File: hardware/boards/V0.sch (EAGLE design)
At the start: 139 parts, among them IC2 TPS6300, J1 SJ-43515TS-SMT, J2 HIROSE_DM3BT-DSF-PEJSHIROSE_D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, J3 MOLEX_105450-0101MOLEX_105450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, Q2 ON_SEMI_MMBT5551LT1GON_SEMI_M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, U1 VS1053-L, U2 MICROCHIP_MCP73831T-2ATI-OTMI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, X3 FH12-45S-0.5SH

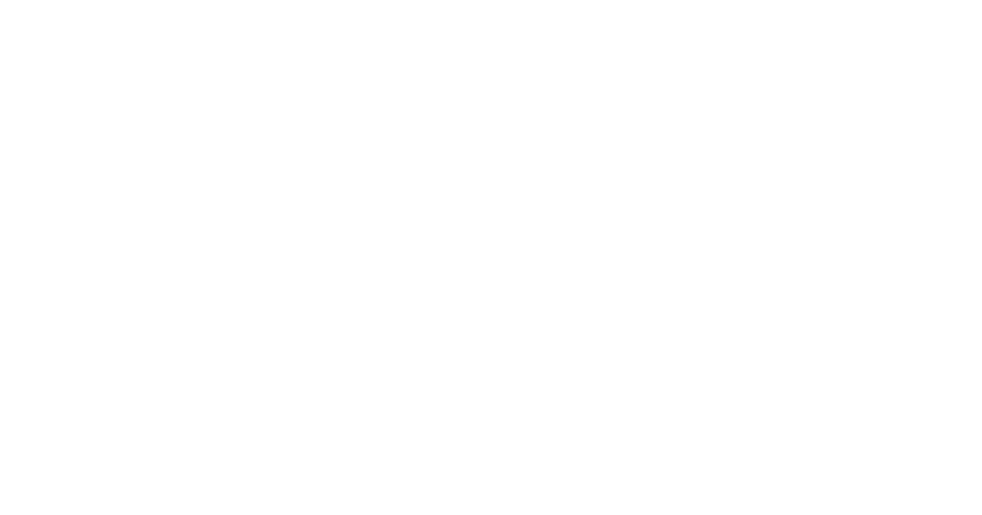
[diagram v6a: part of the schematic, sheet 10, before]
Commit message: Add charge detect back in, using up all our pins
Closes #11
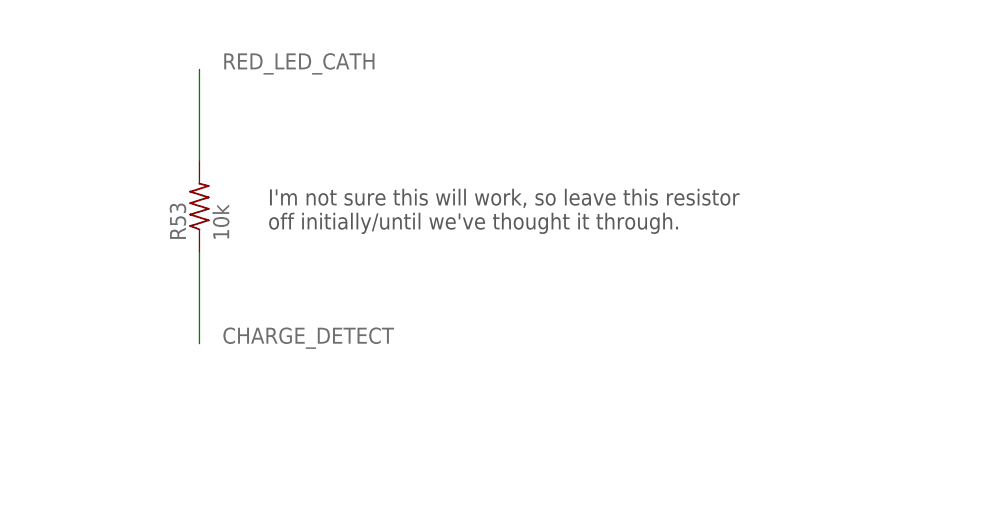
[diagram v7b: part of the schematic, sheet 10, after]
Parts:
- added R53: 10k, rcl:R-US_R0805
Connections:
- new net CHARGE_DETECT: R53.1, U$1.SENSOR_CAPP
- net RED_LED_CATH: now also R53.2
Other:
- note added: "I'm not sure this will work, so leave this resistor off initially/until we've thought it through."
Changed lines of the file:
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@@
 <part name="C36" library="rcl" library_urn="urn:adsk.eagle:library:334" deviceset="C-US" device="C1206" package3d_urn="urn:adsk.eagle:package:23618/2" value="100nF"/>
 <part name="GND48" library="supply1" library_urn="urn:adsk.eagle:library:371" deviceset="GND" device=""/>
+<part name="R53" library="rcl" library_urn="urn:adsk.eagle:library:334" deviceset="R-US_" device="R0805" package3d_urn="urn:adsk.eagle:package:23553/2" value="10k"/>
 </parts>
 <sheets>
@@
 </segment>
 </net>
+<net name="CHARGE_DETECT" class="0">
+<segment>
+<pinref part="U$1" gate="G$1" pin="SENSOR_CAPP"/>
+<wire x1="-50.8" y1="2.54" x2="-55.88" y2="2.54" width="0.1524" layer="91"/>
+<label x="-53.594" y="1.016" size="1.778" layer="95" rot="R180"/>
+</segment>
+</net>
 </nets>
 </sheet>
@@
 1.0 volts for 20mA = V / I = R = 1 / 20mA = 50 ohms</text>
 <text x="-38.1" y="-38.1" size="1.778" layer="97">Blue has a voltage drop of ~3.7V which is greater than our regulated voltage so we won't bother with a current limiting resistor.</text>
+<text x="106.68" y="12.7" size="1.778" layer="97">I'm not sure this will work, so leave this resistor
+off initially/until we've thought it through.</text>
 </plain>
 <instances>
@@
 <attribute name="VALUE" x="-80.518" y="-13.97" size="1.778" layer="96" rot="R90"/>
 </instance>
+<instance part="R53" gate="G$1" x="99.06" y="15.24" smashed="yes" rot="R90">
+<attribute name="NAME" x="97.5614" y="11.43" size="1.778" layer="95" rot="R90"/>
+<attribute name="VALUE" x="102.362" y="11.43" size="1.778" layer="96" rot="R90"/>
+</instance>
 </instances>
 <busses>
@@
 <label x="7.62" y="0" size="1.778" layer="95"/>
 </segment>
+<segment>
+<wire x1="99.06" y1="30.48" x2="99.06" y2="20.32" width="0.1524" layer="91"/>
+<pinref part="R53" gate="G$1" pin="2"/>
+<label x="101.6" y="30.48" size="1.778" layer="95"/>
+</segment>
 </net>
 <net name="N$56" class="0">
@@
 </segment>
 </net>
+<net name="CHARGE_DETECT" class="0">
+<segment>
+<pinref part="R53" gate="G$1" pin="1"/>
+<wire x1="99.06" y1="10.16" x2="99.06" y2="0" width="0.1524" layer="91"/>
+<label x="101.6" y="0" size="1.778" layer="95"/>
+</segment>
+</net>
